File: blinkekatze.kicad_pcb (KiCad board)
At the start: 4 copper layers, 68.1 x 69 mm, 115 parts, among them J1 Power key, J2 Conn_01x06, J3 I2C, Q1 AO3400A, Q2 AO3400A, U1 ESP32-C3-MINI-1, U10 LIS3DH, U2 BQ27546, U3 SRV05-4, U4 FM2113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

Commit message: Partial rip-up of old design
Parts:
- added H10: RU, MountingHole:MountingHole_2.5mm, F.Cu at (117.2, 78.8)
- added H7: LU, MountingHole:MountingHole_2.5mm, F.Cu at (82.8, 78.8)
- added H8: RL, MountingHole:MountingHole_2.5mm, F.Cu at (117.2, 121.3)
- added H9: LL, MountingHole:MountingHole_2.5mm, F.Cu at (82.8, 121.3)
- added R21: 10k, Resistor_SMD:R_0402_1005Metric, F.Cu at (62.0, 80.0)
- added R22: 10k, Resistor_SMD:R_0402_1005Metric, F.Cu at (62.0, 82.0)
- BTT1, BTT2: footprint Battery_Holder_MYOUNG:MY-18650-01 -> Battery_Holder_MYOUNG:MY-18650-01_flat-top
- moved U5 46.8 mm to (116.1, 58.7)
- moved C70 46.8 mm to (118.0, 59.3)
- moved R43 46.8 mm to (114.3, 58.1)
- moved C69 46.8 mm to (116.1, 56.8)
- moved C66 24.0 mm to (68.8, 111.9)
- moved R44 24.0 mm to (69.5, 110.1)
- moved R46 1.02 mm to (86.0, 87.9), turned to 45 degrees
- moved BTT2 0.80 mm to (100.0, 123.6)
- moved U1 0.76 mm to (76.5, 91.2)
- moved C65 0.76 mm to (82.1, 96.6)
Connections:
- U10 pad 11: unconnected-(U10-INT1-Pad11) -> Net-(U1-IO6)
- U10 pad 9: unconnected-(U10-INT2-Pad9) -> Net-(U1-IO7)
- U5 pad 2: Net-(U1-IO9) -> +3V3
- U5 pad 3: Net-(U1-IO7) -> /Battery/SDA
- U5 pad 4: Net-(U1-IO8) -> /Battery/SCL
- U5 pad 5: Net-(U1-IO6) -> Net-(U1-IO8)
- U6 pad 3: Net-(U1-IO5) -> Net-(U1-IO9)
- U7 pad 5: unconnected-(U7-INT-Pad5) -> Net-(U1-IO5)
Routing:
- net Net-(U1-IO5): track 23.4 -> 0.00 mm
- net Net-(U1-IO9): track 3.82 -> 22.2 mm, vias 0 -> 1
- net /Logic/USB_D-: track 15.2 -> 3.31 mm, vias 2 -> 0
- net /Logic/USB_D+: track 16.4 -> 6.11 mm
- net Net-(U1-IO6): track 9.31 -> 0.00 mm
- net /Battery/SCL: track 104.8 -> 95.7 mm
- net GND: track 124.5 -> 119.2 mm, vias 99 -> 97
- net +3V3: track 47.5 -> 42.5 mm, vias 18 -> 14
- net /Battery/SDA: track 102.7 -> 97.9 mm
- net /LEDs/DIN: track 6.51 -> 1.78 mm
- net Net-(U1-EN): track 2.44 -> 0.00 mm
- net /Charger/~{CHARGE_ENABLE}: track 49.6 -> 47.5 mm
- net Net-(U1-IO10): track 18.1 -> 16.4 mm
- net Net-(U1-IO4): track 21.3 -> 19.7 mm
- net Net-(U1-IO8): track 1.24 -> 0.00 mm
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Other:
- board text added: "TODO: - fix battery length - fix ESP module position (collides with diffuser) - adjust PCB shape to cover left lower mounting hole - Replace pin header with FFC connector - Expose IO9 and reset strapping pins on unpopulated header (force bootloader) - Move barometer to I2C bus"

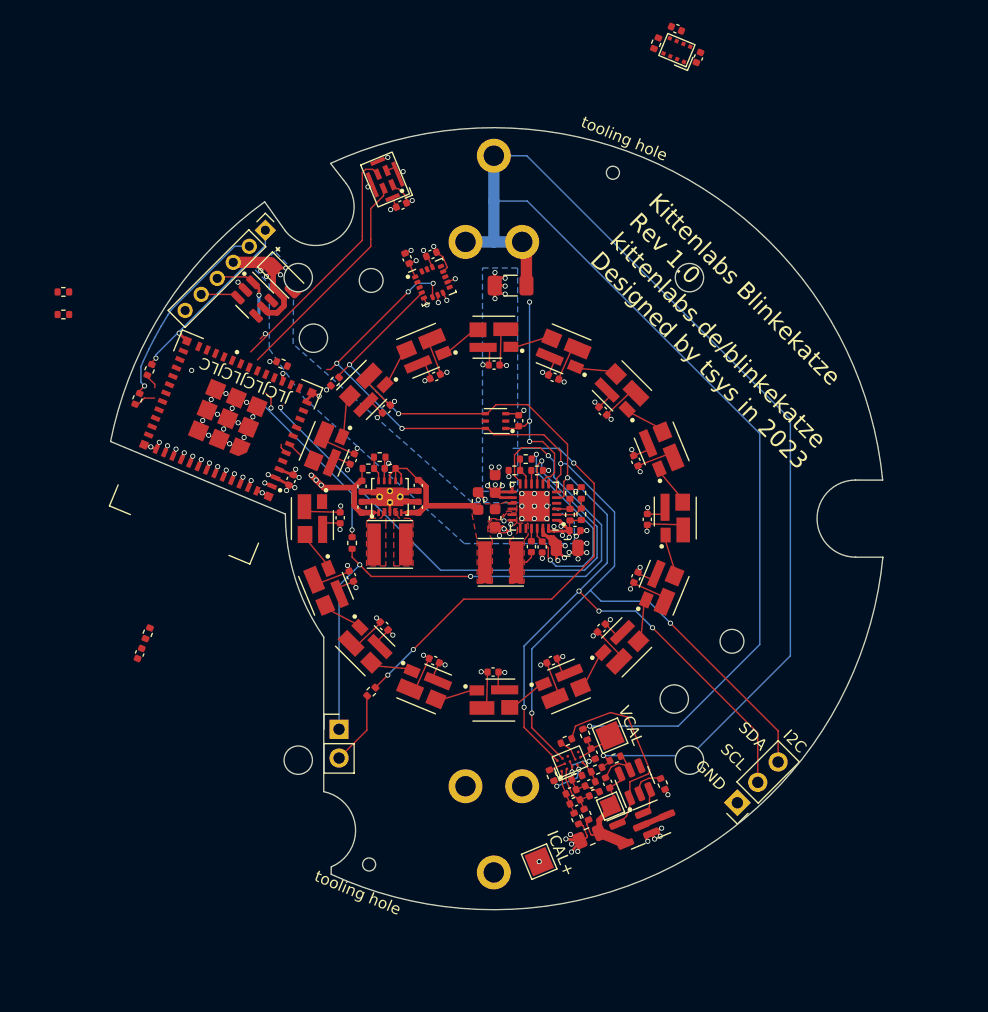
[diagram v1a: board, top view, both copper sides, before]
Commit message: Relayout board to fit constraints of Micro USB Blinkekatzen
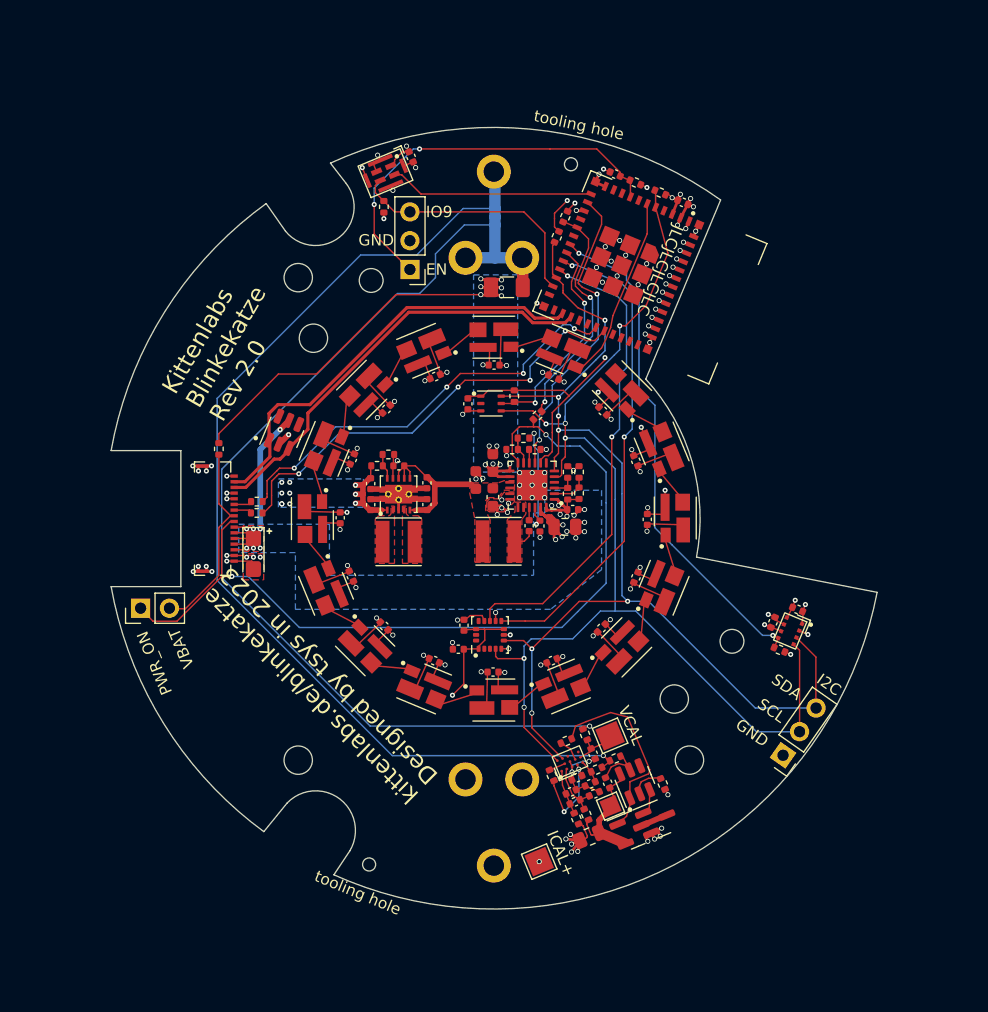
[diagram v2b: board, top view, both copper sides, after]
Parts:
- removed H10: RU, MountingHole:MountingHole_2.5mm
- added J4: USB board, Connector_FFC-FPC_HDGC:0.5K-QX-16PWB_16Pin_0.5mm, F.Cu at (77.1, 100.0)
- added R23: 100k, Resistor_SMD:R_0402_1005Metric, F.Cu at (106.3, 73.4)
- J2: value Conn_01x06 -> Strapping; footprint Connector_PinHeader_2.00mm:PinHeader_1x06_P2.00mm_Vertical -> Connector_PinHeader_2.54mm:PinHeader_1x03_P2.54mm_Vertical
- moved R21 70.6 mm to (125.2, 111.6), turned to 157.5 degrees
- moved C66 59.5 mm to (110.7, 69.6), turned to -22.5 degrees
- moved R44 58.6 mm to (112.5, 70.4), turned to 157.5 degrees
- moved C69 53.0 mm to (124.6, 109.1), turned to -112.5 degrees
- moved U5 52.2 mm to (126.1, 109.9), turned to -112.5 degrees
- moved C70 49.5 mm to (126.8, 108.0), turned to -22.5 degrees
- moved C65 42.3 mm to (116.7, 72.1), turned to -22.5 degrees
- moved R22 40.4 mm to (101.8, 89.2), turned to -90 degrees
- moved U1 37.3 mm to (111.3, 77.7), turned to -112.5 degrees
- moved C18 34.8 mm to (96.9, 111.5), turned to 0 degrees
- moved R46 33.2 mm to (114.7, 71.2), turned to 157.5 degrees
- moved C19 32.8 mm to (97.4, 109.4), turned to 90 degrees
- moved U10 31.5 mm to (99.7, 110.3), turned to 90 degrees
- moved R43 28.0 mm to (90.3, 72.5), turned to 90 degrees
- moved R45 26.7 mm to (105.5, 75.2), turned to -112.5 degrees
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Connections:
- C32 pad 1: /VBAT -> /Battery/BAT+
- C66 pad 2: Net-(U1-EN) -> /Logic/EN
- D1 pad 1: /LEDs/DIN -> Net-(D1-DIN)
- D11 pad 3: Net-(D11-DOUT) -> unconnected-(D11-DOUT-Pad3)
- D12 pad 1: Net-(D11-DOUT) -> /LEDs/DIN
- D16 pad 3: unconnected-(D16-DOUT-Pad3) -> Net-(D1-DIN)
- F1 pad 2: /VBAT -> /Battery/BAT+
- J1 pad 2: Net-(J1-Pin_2) -> /USB/VBAT
- J2 pad 1: /Logic/LED1 -> /Logic/EN
- J2 pad 2: /Logic/LED2 -> GND
- J2 pad 3: VBUS -> /Logic/IO9
- R2 pad 1: /VBAT -> /USB/VBAT
- R2 pad 2: Net-(J1-Pin_2) -> /Battery/BAT+
- R21 pad 2: Net-(U1-IO8) -> Net-(U1-IO4)
- R43 pad 2: Net-(U1-IO9) -> /Logic/IO9
- R44 pad 2: Net-(U1-EN) -> /Logic/EN
- U1 pad 12: /Battery/SDA -> Net-(U1-IO0)
- U1 pad 22: Net-(U1-IO8) -> /Battery/SDA
- U1 pad 23: Net-(U1-IO9) -> /Logic/IO9
- U1 pad 8: Net-(U1-EN) -> /Logic/EN
- U10 pad 11: Net-(U1-IO6) -> Net-(U1-IO7)
- U10 pad 9: Net-(U1-IO7) -> Net-(U1-IO6)
- U3 pad 1: /Logic/USB_D+ -> /Logic/USB_D-
- U3 pad 3: /Logic/USB_D- -> /Logic/USB_D+
- U5 pad 5: Net-(U1-IO8) -> Net-(U1-IO4)
- U6 pad 3: Net-(U1-IO9) -> /Logic/IO9
- U6 pad 4: Net-(U1-IO4) -> Net-(U1-IO0)
- U8 pad 13: /VBAT -> /Battery/BAT+
- U8 pad 14: /VBAT -> /Battery/BAT+
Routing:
- net /VBAT: track 50.3 -> 0.00 mm, vias 12 -> 0
- net Net-(U1-IO6): track 0.00 -> 42.7 mm, vias 0 -> 2
- net Net-(U1-IO7): track 0.00 -> 42.1 mm, vias 0 -> 2
- net /Battery/BAT+: track 0.00 -> 40.8 mm, vias 0 -> 10
- net Net-(U1-TXD0): track 2.02 -> 39.3 mm, vias 0 -> 4
- net Net-(U1-RXD0): track 1.37 -> 37.7 mm, vias 0 -> 4
- net /Logic/EN: track 0.00 -> 35.3 mm, vias 0 -> 2
- net /Logic/USB_D-: track 3.31 -> 38.3 mm
- net /Logic/USB_D+: track 6.11 -> 37.4 mm, vias 2 -> 0
- net Net-(U1-IO4): track 19.7 -> 44.9 mm, vias 0 -> 2
- net +BATT: track 164.5 -> 187.3 mm
- net /Logic/IO9: track 0.00 -> 22.7 mm
- net Net-(U1-IO9): track 22.2 -> 0.00 mm, vias 1 -> 0
- net /Charger/~{CHARGE_ENABLE}: track 47.5 -> 27.2 mm
- net Net-(U1-IO5): track 0.00 -> 19.2 mm, vias 0 -> 2
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- added copper zone on B.Cu, net +3V3
- added copper zone on B.Cu, net /Battery/BAT+
- added copper zone on F.Cu, net VBUS
- removed copper zone on B.Cu, net /VBAT
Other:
- board size 68.1 x 69 mm -> 67.6 x 68.9 mm
- board text added: "EN"
- board text added: "IO9"
- board text added: "Kittenlabs Blinkekatze Rev 2.0"
- board text added: "kittenlabs.de/blinkekatze Designed by tsys in 2023"
- board text removed: "D+"
- board text removed: "D-"
- board text removed: "Kittenlabs Blinkekatze Rev 1.0 kittenlabs.de/blinkekatze Designed by tsys in 2023"
- board text removed: "LED1"
- board text removed: "LED2"
- board text removed: "TODO: - fix battery length - fix ESP module position (collides with diffuser) - adjust PCB shape to cover left lower mounting hole - Replace pin header with FFC connector - Expose IO9 and reset strapping pins on unpopulated header (force bootloader) - Move barometer to I2C bus"
- board text removed: "VBUS"

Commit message: DFM and 2A input current limit
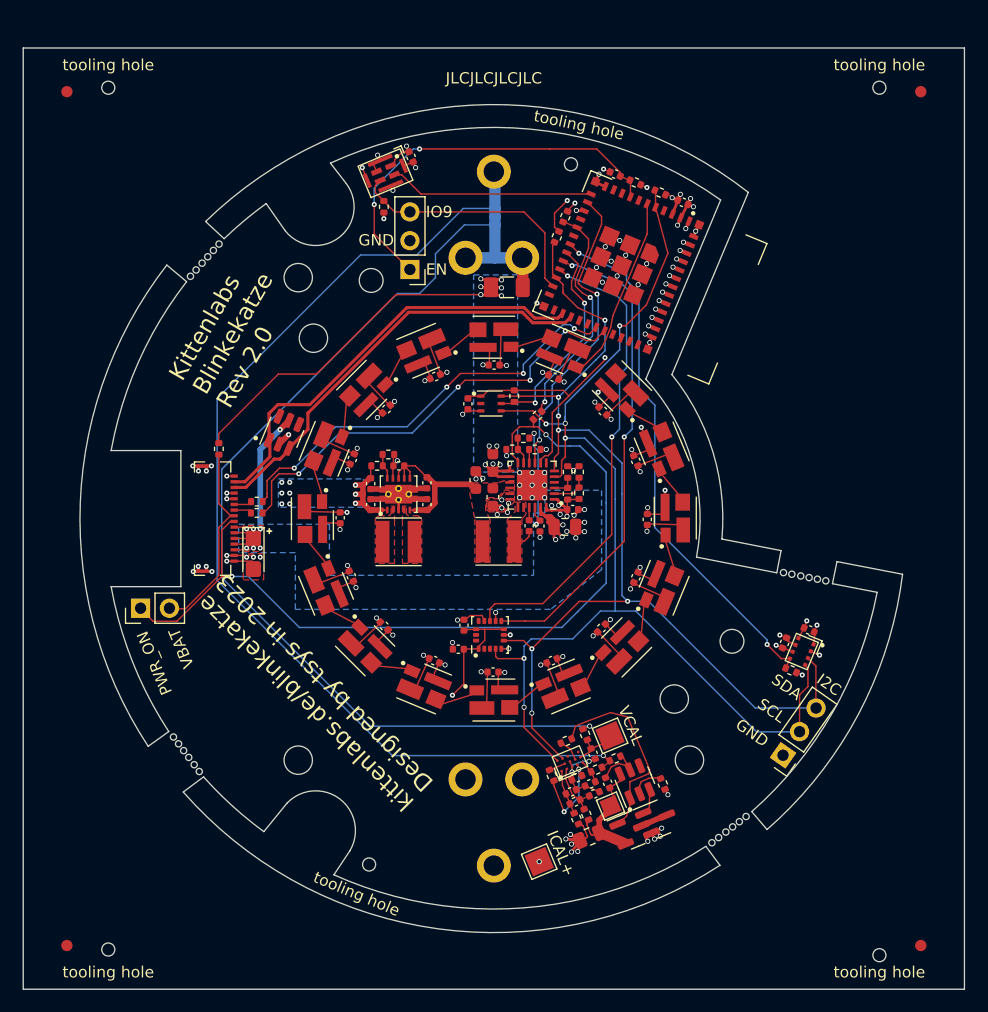
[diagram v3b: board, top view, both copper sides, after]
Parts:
- added REF**: MouseBites_JLCSMT, ToolingHole:MouseBites_JLCSMT, F.Cu at (72.9, 120.8)
- added REF**: MouseBites_JLCSMT, ToolingHole:MouseBites_JLCSMT, F.Cu at (120.8, 127.4)
- added REF**: Fiducial_JLCSMT, ToolingHole:Fiducial_JLCSMT, F.Cu at (137.7, 137.7)
- added REF**: ToolingHole_JLCSMT, ToolingHole:ToolingHole_JLCSMT, F.Cu at (66.0, 138.0)
- added REF**: MouseBites_JLCSMT, ToolingHole:MouseBites_JLCSMT, F.Cu at (74.5, 77.2)
- added REF**: ToolingHole_JLCSMT, ToolingHole:ToolingHole_JLCSMT, F.Cu at (134.0, 138.5)
- added REF**: Fiducial_JLCSMT, ToolingHole:Fiducial_JLCSMT, F.Cu at (62.4, 137.7)
- added REF**: Fiducial_JLCSMT, ToolingHole:Fiducial_JLCSMT, F.Cu at (62.4, 62.4)
- added REF**: ToolingHole_JLCSMT, ToolingHole:ToolingHole_JLCSMT, F.Cu at (66.0, 62.0)
- added REF**: ToolingHole_JLCSMT, ToolingHole:ToolingHole_JLCSMT, F.Cu at (134.0, 62.0)
- added REF**: Fiducial_JLCSMT, ToolingHole:Fiducial_JLCSMT, F.Cu at (137.7, 62.4)
- added REF**: MouseBites_JLCSMT, ToolingHole:MouseBites_JLCSMT, F.Cu at (127.4, 105.1)
- R3: value 150R -> 220R
- moved C69 2.08 mm to (125.6, 111.0)
- moved C70 2.08 mm to (127.8, 109.8)
- moved U5 2.08 mm to (127.2, 111.7)
- moved R21 2.08 mm to (126.2, 113.4)
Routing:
- net /Battery/SDA: track 100.0 -> 97.7 mm
- net Net-(U1-IO4): track 44.9 -> 47.0 mm
- net /Battery/SCL: track 107.0 -> 105.5 mm
- net +3V3: vias 22 -> 21
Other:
- board size 67.6 x 68.9 mm -> 83 x 83 mm
